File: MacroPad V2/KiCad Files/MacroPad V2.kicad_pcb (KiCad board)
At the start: 2 copper layers, 119.2 x 96 mm, 17 parts, among them SW1 RotaryEncoder_Switch, SW2 RotaryEncoder_Switch, SW3 RotaryEncoder_Switch, U1 Pico

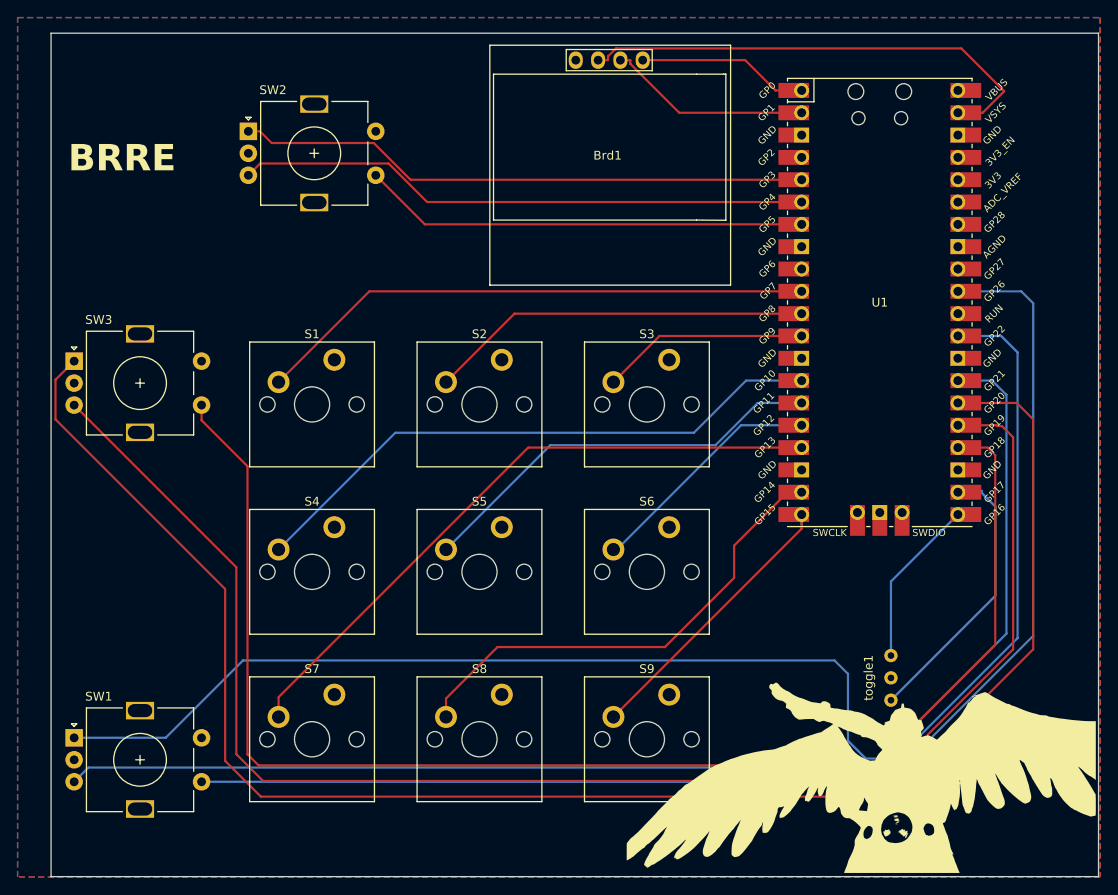
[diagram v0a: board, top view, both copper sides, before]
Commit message: Rewired to avoid pins
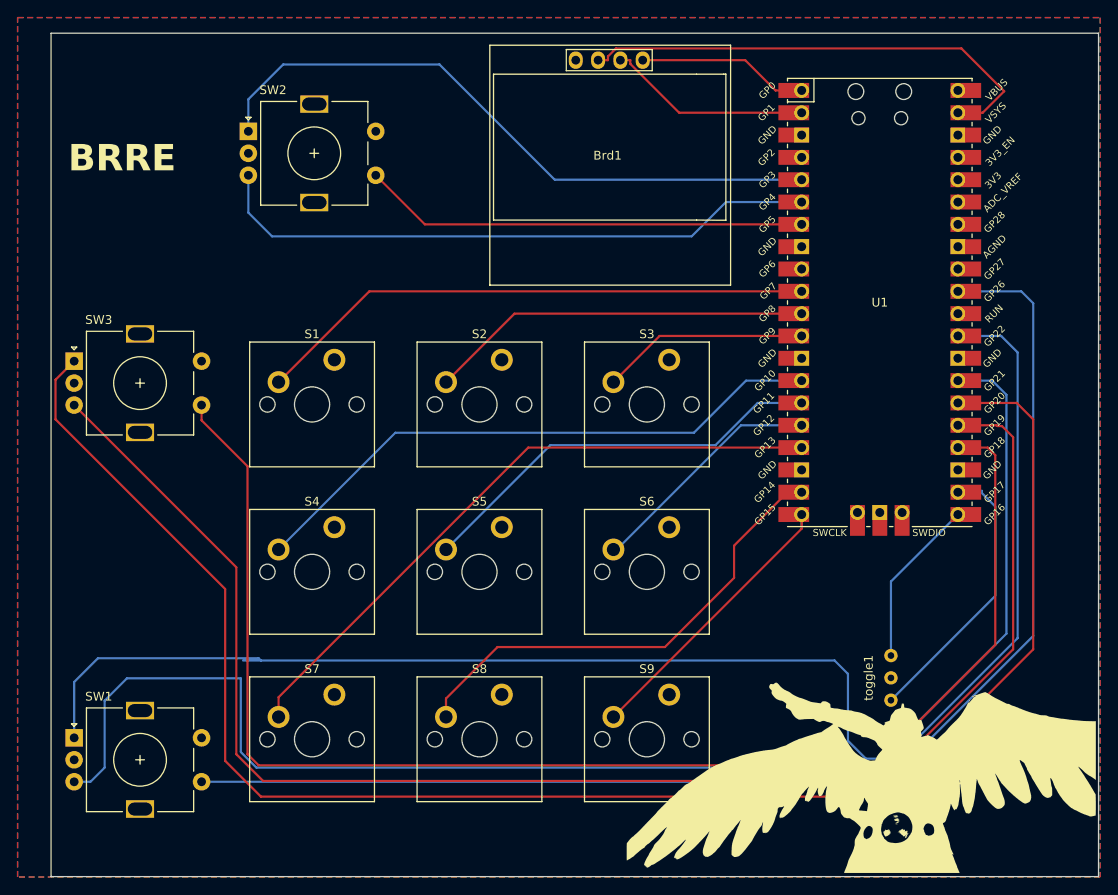
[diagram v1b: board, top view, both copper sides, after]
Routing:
- net B1: track 154.2 -> 172.0 mm
- net A2: track 65.2 -> 73.7 mm
- net A1: track 158.1 -> 164.1 mm
- net B2: track 65.3 -> 69.9 mm
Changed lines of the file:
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@@
     )
     (pad_to_mask_clearance 0)
-    (grid_origin 187.452 102.87)
+    (grid_origin 88.392 67.31)
     (pcbplotparams
       (layerselection 0x00010fc_ffffffff)
@@
       (drillshape 0)
       (scaleselection 1)
-      (outputdirectory "../")
+      (outputdirectory "../Gerber/")
     )
   )
@@
   (segment (start 166.182 110.652) (end 166.182 111.829) (width 0.25) (layer "B.Cu") (net 14))
   (segment (start 144.762 133.249) (end 144.762 133.682) (width 0.25) (layer "B.Cu") (net 14))
+  (segment (start 104.648 127.254) (end 169.926 127.254) (width 0.25) (layer "B.Cu") (net 15))
   (segment (start 83.3975 136.06) (end 83.397 136.06) (width 0.25) (layer "B.Cu") (net 15))
   (segment (start 189.484 97.028) (end 187.868 95.412) (width 0.25) (layer "B.Cu") (net 15))
   (segment (start 171.45 128.778) (end 171.45 136.398) (width 0.25) (layer "B.Cu") (net 15))
-  (segment (start 93.8105 136.0595) (end 102.616 127.254) (width 0.25) (layer "B.Cu") (net 15))
   (segment (start 83.3975 136.06) (end 83.397 136.0595) (width 0.25) (layer "B.Cu") (net 15))
   (segment (start 171.45 136.398) (end 173.482 138.43) (width 0.25) (layer "B.Cu") (net 15))
@@
   (segment (start 187.868 95.412) (end 183.962 95.412) (width 0.25) (layer "B.Cu") (net 15))
   (segment (start 189.484 124.206) (end 189.484 97.028) (width 0.25) (layer "B.Cu") (net 15))
-  (segment (start 102.616 127.254) (end 169.926 127.254) (width 0.25) (layer "B.Cu") (net 15))
-  (segment (start 83.397 136.0595) (end 93.8105 136.0595) (width 0.25) (layer "B.Cu") (net 15))
+  (segment (start 83.397 129.709) (end 86.106 127) (width 0.25) (layer "B.Cu") (net 15))
+  (segment (start 83.397 136.0595) (end 83.397 129.709) (width 0.25) (layer "B.Cu") (net 15))
+  (segment (start 86.106 127) (end 104.394 127) (width 0.25) (layer "B.Cu") (net 15))
+  (segment (start 102.616 127.254) (end 104.648 127.254) (width 0.25) (layer "B.Cu") (net 15))
+  (segment (start 104.394 127) (end 104.648 127.254) (width 0.25) (layer "B.Cu") (net 15))
   (segment (start 175.26 138.43) (end 189.484 124.206) (width 0.25) (layer "B.Cu") (net 15))
   (segment (start 83.3971 141.0595) (end 83.3974 141.0598) (width 0.25) (layer "F.Cu") (net 16))
   (segment (start 83.397 141.0595) (end 83.3971 141.0595) (width 0.25) (layer "F.Cu") (net 16))
   (segment (start 83.3974 141.0598) (end 83.3972 141.06) (width 0.25) (layer "F.Cu") (net 16))
+  (segment (start 85.2545 141.0595) (end 83.397 141.0595) (width 0.25) (layer "B.Cu") (net 16))
   (segment (start 190.754 92.202) (end 190.754 124.714) (width 0.25) (layer "B.Cu") (net 16))
+  (segment (start 86.868 139.446) (end 85.2545 141.0595) (width 0.25) (layer "B.Cu") (net 16))
+  (segment (start 176.022 139.446) (end 104.14 139.446) (width 0.25) (layer "B.Cu") (net 16))
+  (segment (start 86.868 131.826) (end 86.868 139.446) (width 0.25) (layer "B.Cu") (net 16))
   (segment (start 190.754 124.714) (end 176.022 139.446) (width 0.25) (layer "B.Cu") (net 16))
-  (segment (start 85.0105 139.446) (end 83.397 141.0595) (width 0.25) (layer "B.Cu") (net 16))
-  (segment (start 176.022 139.446) (end 85.0105 139.446) (width 0.25) (layer "B.Cu") (net 16))
+  (segment (start 104.14 139.446) (end 102.362 137.668) (width 0.25) (layer "B.Cu") (net 16))
+  (segment (start 102.362 129.286) (end 89.408 129.286) (width 0.25) (layer "B.Cu") (net 16))
+  (segment (start 102.362 137.668) (end 102.362 129.286) (width 0.25) (layer "B.Cu") (net 16))
   (segment (start 183.962 90.332) (end 188.884 90.332) (width 0.25) (layer "B.Cu") (net 16))
+  (segment (start 89.408 129.286) (end 86.868 131.826) (width 0.25) (layer "B.Cu") (net 16))
   (segment (start 188.884 90.332) (end 190.754 92.202) (width 0.25) (layer "B.Cu") (net 16))
   (segment (start 191.17 85.252) (end 183.962 85.252) (width 0.25) (layer "B.Cu") (net 17))
@@
   (segment (start 175.9325 141.0595) (end 192.532 124.46) (width 0.25) (layer "B.Cu") (net 17))
   (segment (start 192.532 86.614) (end 191.17 85.252) (width 0.25) (layer "B.Cu") (net 17))
-  (segment (start 104.549 67.047) (end 105.876 68.3739) (width 0.25) (layer "F.Cu") (net 18))
-  (segment (start 103.222 67.047) (end 104.549 67.047) (width 0.25) (layer "F.Cu") (net 18))
-  (segment (start 117.493 68.3739) (end 121.671 72.552) (width 0.25) (layer "F.Cu") (net 18))
-  (segment (start 105.876 68.3739) (end 117.493 68.3739) (width 0.25) (layer "F.Cu") (net 18))
-  (segment (start 121.671 72.552) (end 166.182 72.552) (width 0.25) (layer "F.Cu") (net 18))
-  (segment (start 103.222 72.047) (end 104.562 70.7067) (width 0.25) (layer "F.Cu") (net 19))
-  (segment (start 119.187 70.7067) (end 123.572 75.092) (width 0.25) (layer "F.Cu") (net 19))
-  (segment (start 123.572 75.092) (end 166.182 75.092) (width 0.25) (layer "F.Cu") (net 19))
-  (segment (start 104.562 70.7067) (end 119.187 70.7067) (width 0.25) (layer "F.Cu") (net 19))
+  (segment (start 138.084 72.552) (end 166.182 72.552) (width 0.25) (layer "B.Cu") (net 18))
+  (segment (start 124.968 59.436) (end 138.084 72.552) (width 0.25) (layer "B.Cu") (net 18))
+  (segment (start 107.188 59.436) (end 124.968 59.436) (width 0.25) (layer "B.Cu") (net 18))
+  (segment (start 103.222 67.047) (end 103.222 63.402) (width 0.25) (layer "B.Cu") (net 18))
+  (segment (start 103.222 63.402) (end 107.188 59.436) (width 0.25) (layer "B.Cu") (net 18))
+  (segment (start 166.182 75.092) (end 157.572 75.092) (width 0.25) (layer "B.Cu") (net 19))
+  (segment (start 153.67 78.994) (end 105.918 78.994) (width 0.25) (layer "B.Cu") (net 19))
+  (segment (start 105.918 78.994) (end 103.222 76.298) (width 0.25) (layer "B.Cu") (net 19))
+  (segment (start 157.572 75.092) (end 153.67 78.994) (width 0.25) (layer "B.Cu") (net 19))
+  (segment (start 103.222 76.298) (end 103.222 72.047) (width 0.25) (layer "B.Cu") (net 19))
   (segment (start 166.182 77.632) (end 123.307 77.632) (width 0.25) (layer "F.Cu") (net 20))
   (segment (start 123.307 77.632) (end 117.722 72.047) (width 0.25) (layer "F.Cu") (net 20))
